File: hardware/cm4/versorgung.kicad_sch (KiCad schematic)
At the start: 7 parts, among them J10 USB-C 5V/USB, U10 USBLC6-2SC6

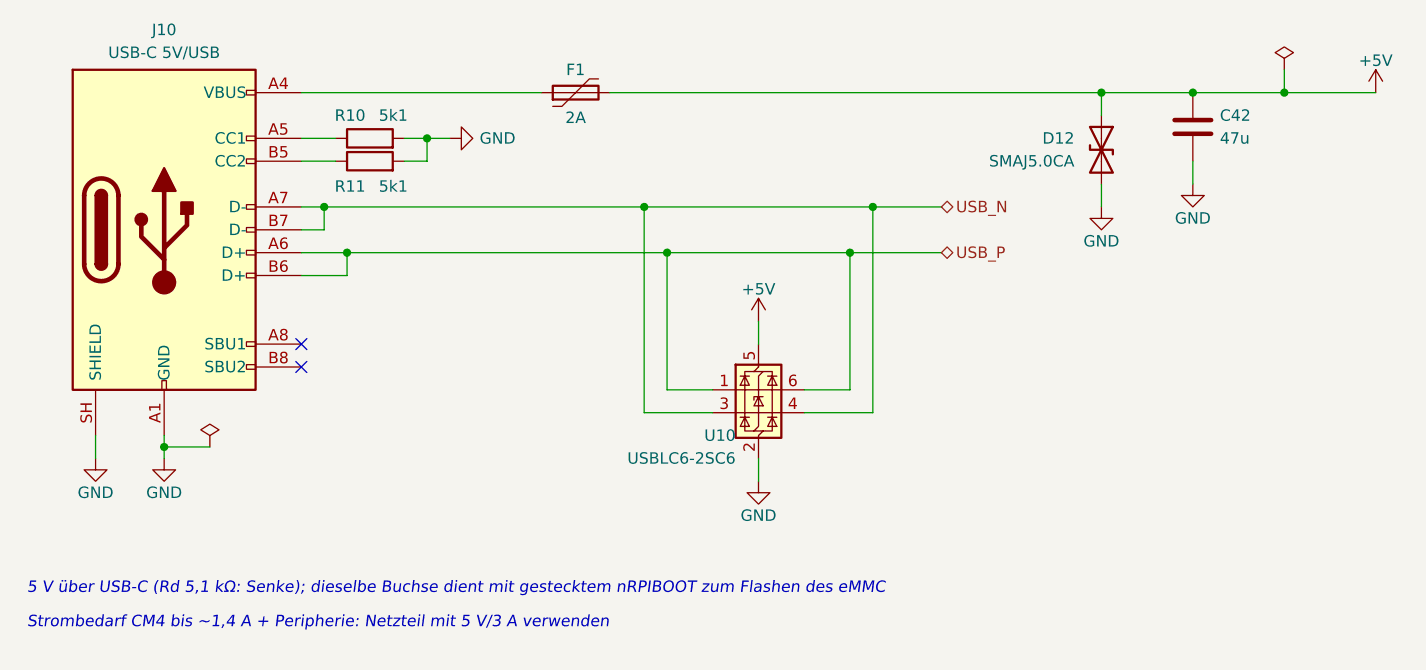
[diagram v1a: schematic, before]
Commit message: Schaltplan: Hinweise als Textkästen (KiCad bricht um); Texte werden in den Generator zurückgeführt
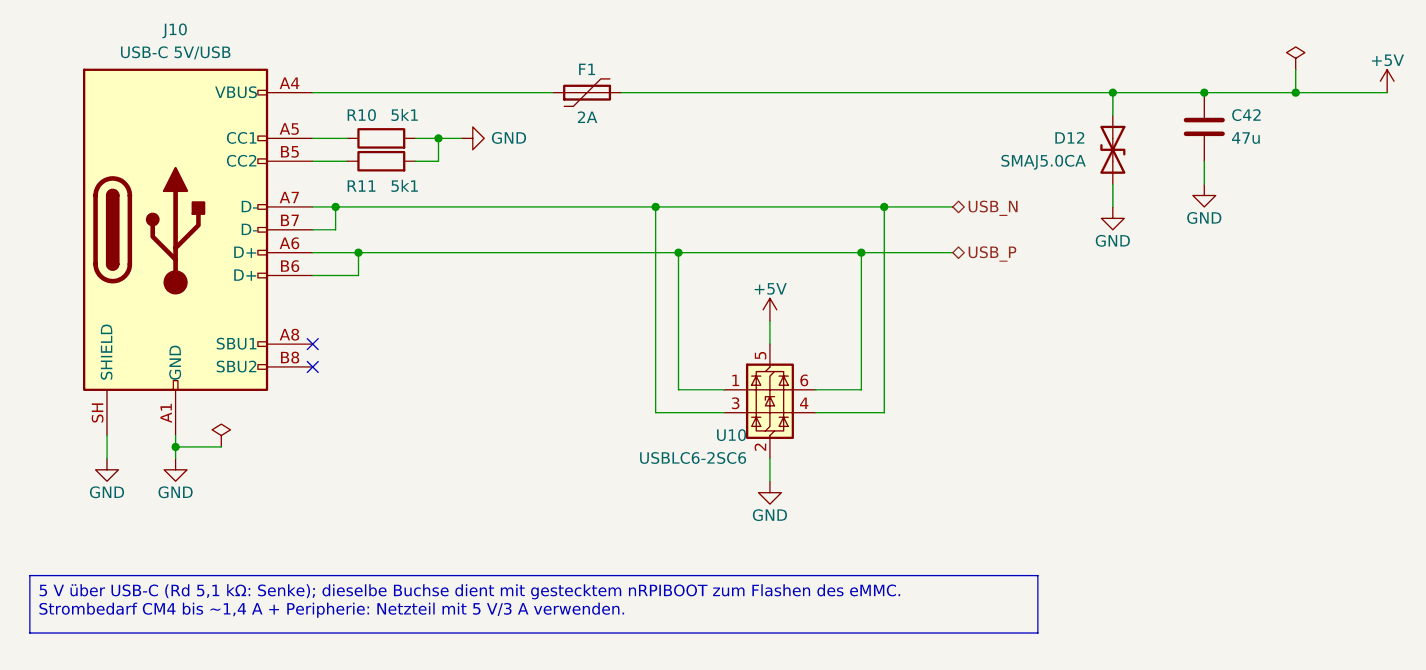
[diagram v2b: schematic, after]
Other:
- note removed: "5 V über USB-C (Rd 5,1 kΩ: Senke); dieselbe Buchse dient mit gestecktem nRPIBOOT zum Flashen des eMMC"
- note removed: "Strombedarf CM4 bis ~1,4 A + Peripherie: Netzteil mit 5 V/3 A verwenden"
- moved on the sheet: C42, D12, F1, J10, R10, R11, U10

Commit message: CM4-Schaltplan: Handänderungen übernommen (Handlage für 8 Blätter, 2 Texte zurückgeführt); Kastenhöhen aus gemessenen Zeichenbreiten
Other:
- moved on the sheet: C42, D12, F1, J10, R10, R11, U10
